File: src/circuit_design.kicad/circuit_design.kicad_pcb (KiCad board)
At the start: 2 copper layers, 220.3 x 182.9 mm, 184 parts, among them J1 CONN_BAT, Q1 BT136-600, Q2 BT136-600, Q3 BT136-600, Q4 BT136-600, U1 К176ИЕ12, U10 К155ЛА4, U11 К155ЛИ1, U12 К155ЛА1, U13 К155ИЕ5, U14 К155ЛЛ1, U15 К155ЛН1, U16 К155ЛИ1, U17 К155ТВ15, U18 К155ИЕ5, U19 К155ЛП5, U2 К155ЛП10, U20 К155ИВ1, U21 К155ИД7, U22 К155ИД4, U23 К155ЛН1, U24 К155ЛП10, U25 MOC3062M, U26 MOC3062M, U27 MOC3062M, U28 MOC3062M, U29 LM7806_TO220, U3 К155ЛЕ3, U30 SC6038, U31 К155ЛЕ1, U32 К155ЛН1, U33 К155ЛИ1, U34 К155ЛА4, U35 К155ТВ15, U36 К155ТЛ2, U37 4020, U38 LM7806_TO220, U39 К155ЛН1, U4 К155ЛН1, U5 К155ЛИ1, U6 К155ЛЛ1, U7 4020, U8 ICL7660, U9 К155ИЕ5, Y1 32768

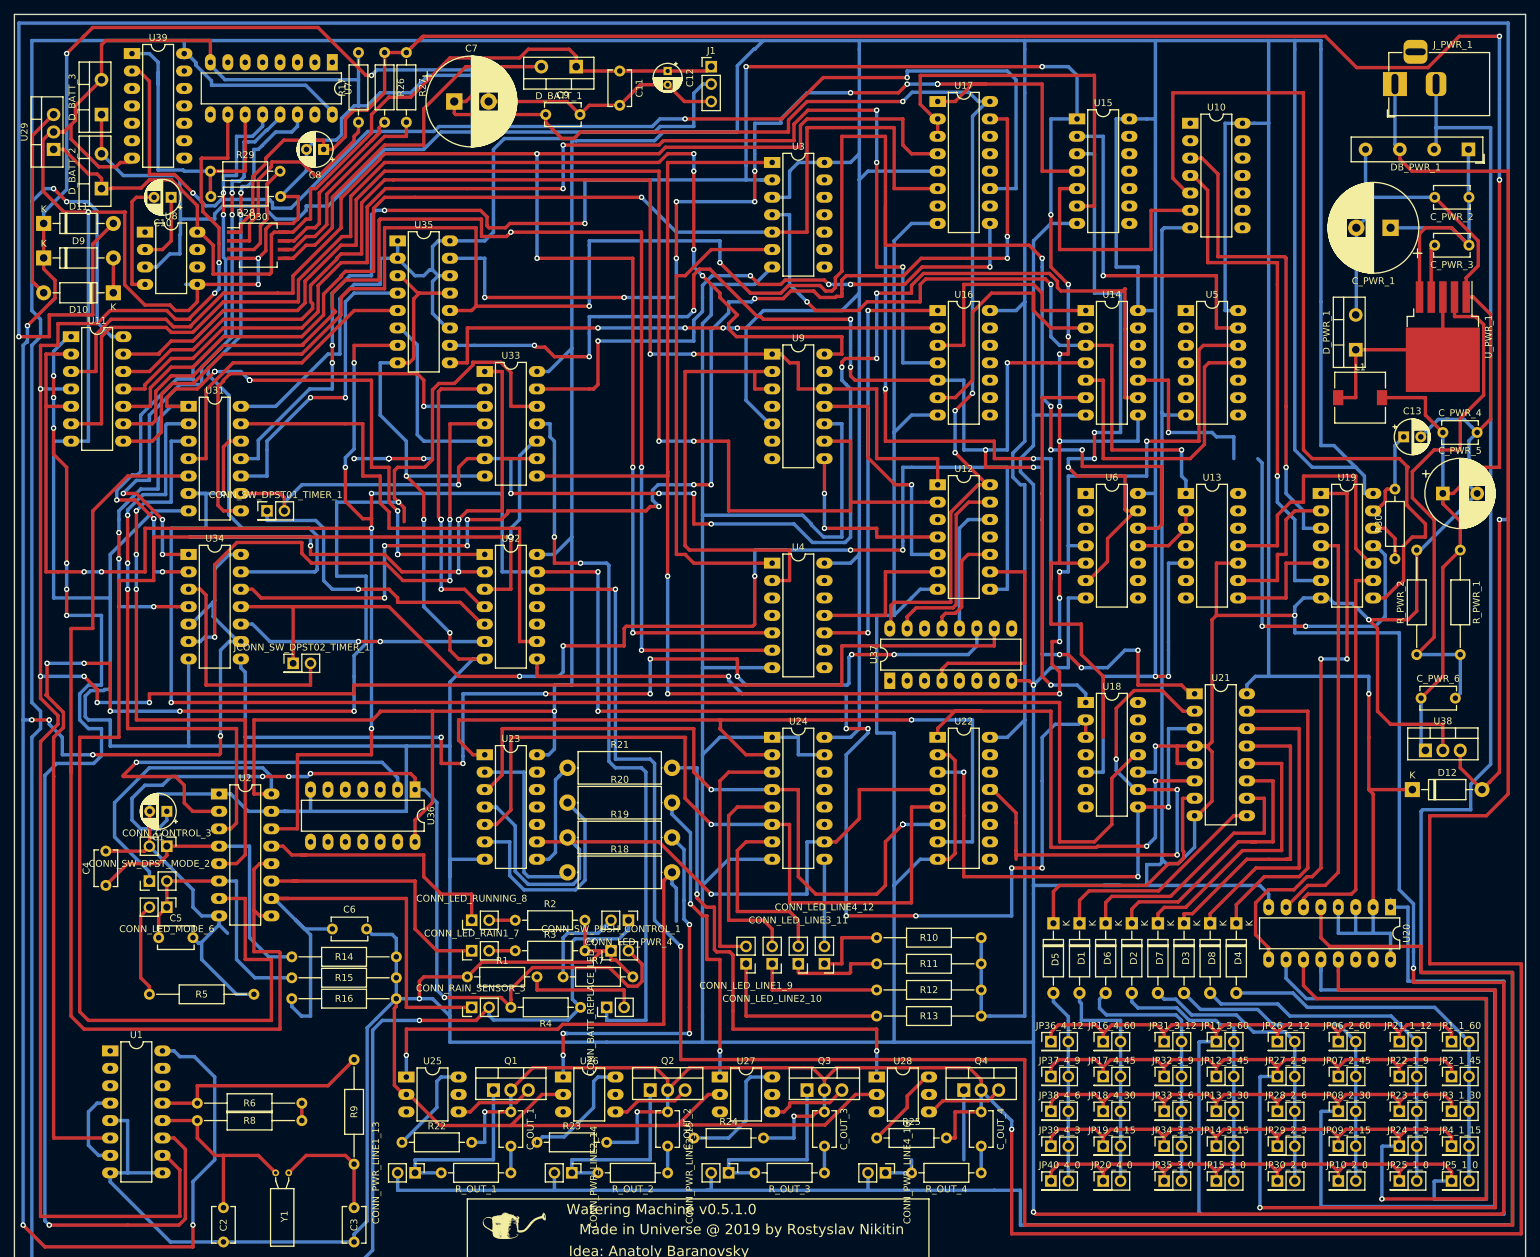
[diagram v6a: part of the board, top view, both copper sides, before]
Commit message: The PCB layout was fixed according to the rules.
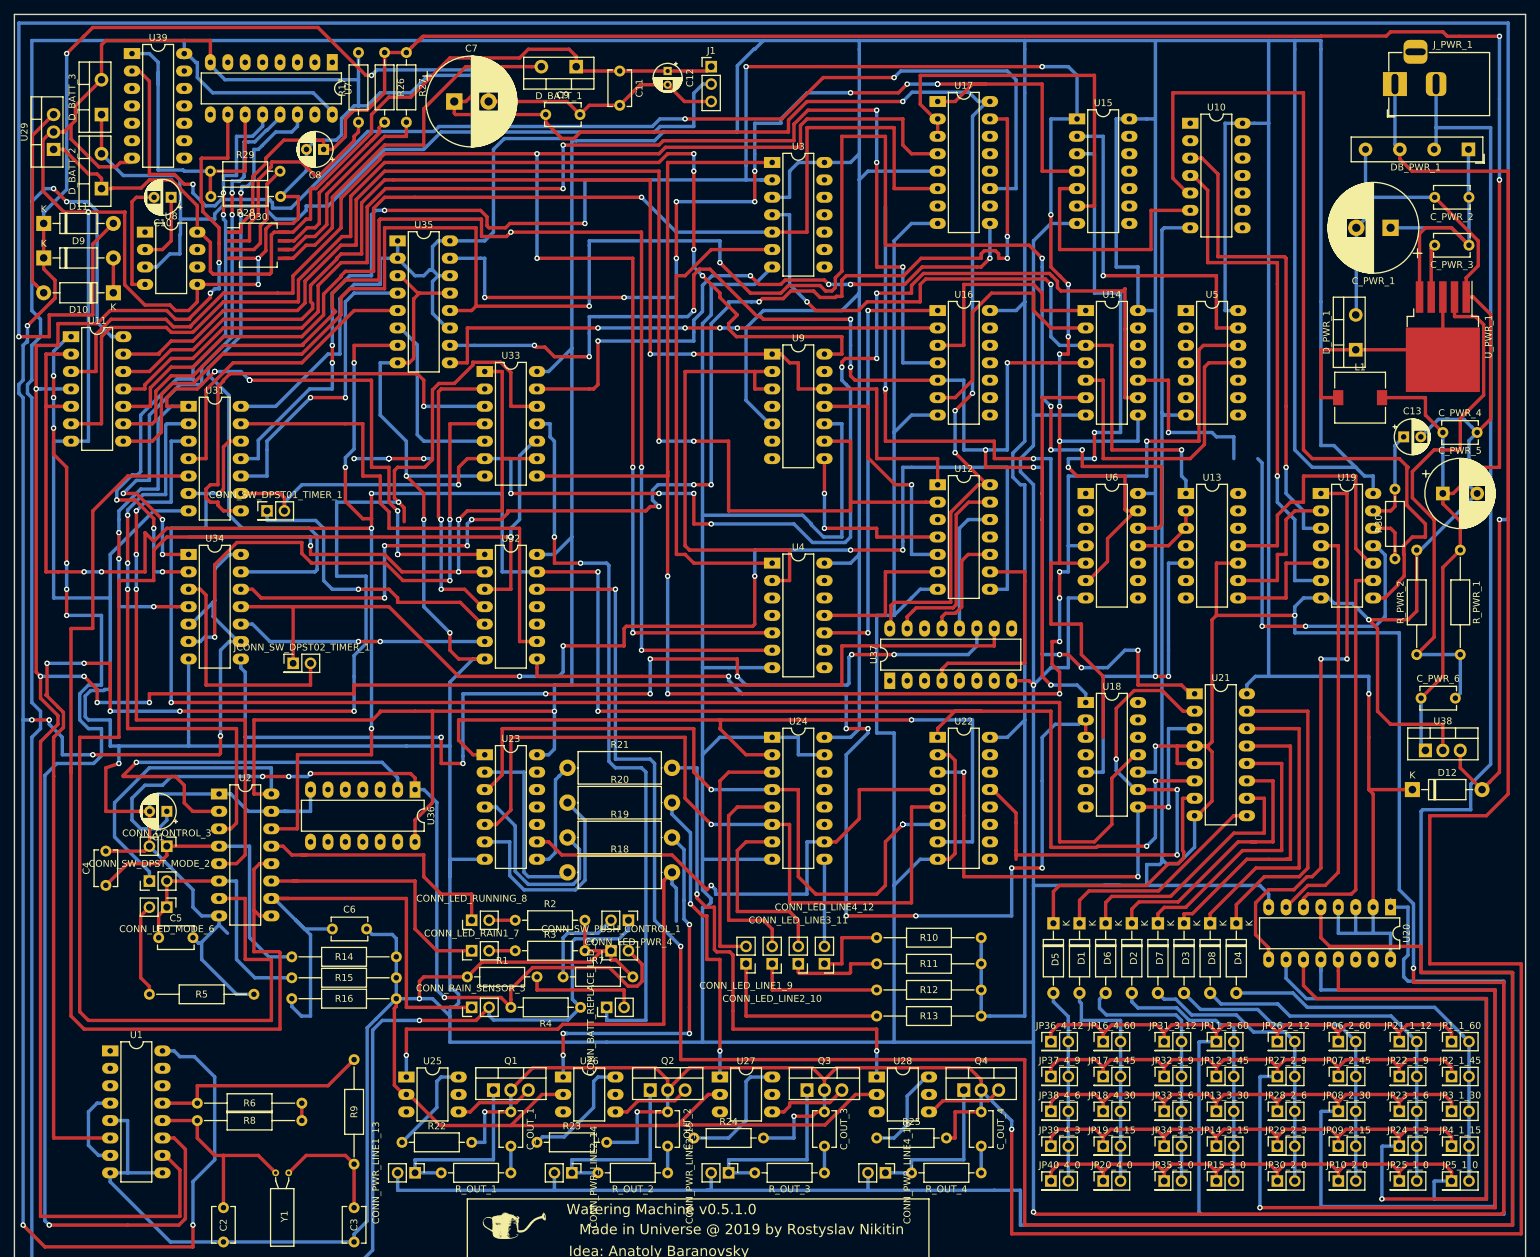
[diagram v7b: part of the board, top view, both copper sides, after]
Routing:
- net Net-(CONN_PWR_LINE4_16-Pad1): track 15.9 -> 23.5 mm
- net GND: track 2175.5 -> 2169.2 mm, vias 13 -> 14
- net Net-(D_PWR_1-Pad1): track 32.0 -> 37.1 mm
- net +9V: track 347.4 -> 344.1 mm
- net /Completed(In): track 223.3 -> 220.4 mm
- net Net-(U31-Pad8): track 64.9 -> 67.7 mm
- net +5V: track 1810.6 -> 1812.5 mm
- net CLK_MIN: track 379.4 -> 381.1 mm
- net Net-(R25-Pad1): track 12.3 -> 13.8 mm
- net Net-(U17-Pad15): track 182.0 -> 183.3 mm
- net Net-(U10-Pad5): track 128.9 -> 130.1 mm
- net /Mode(In): track 213.2 -> 212.0 mm
- net Net-(U22-Pad4): track 74.8 -> 75.7 mm
- net Net-(U17-Pad9): track 90.3 -> 89.6 mm
- net /Running(Out): track 380.0 -> 380.7 mm
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
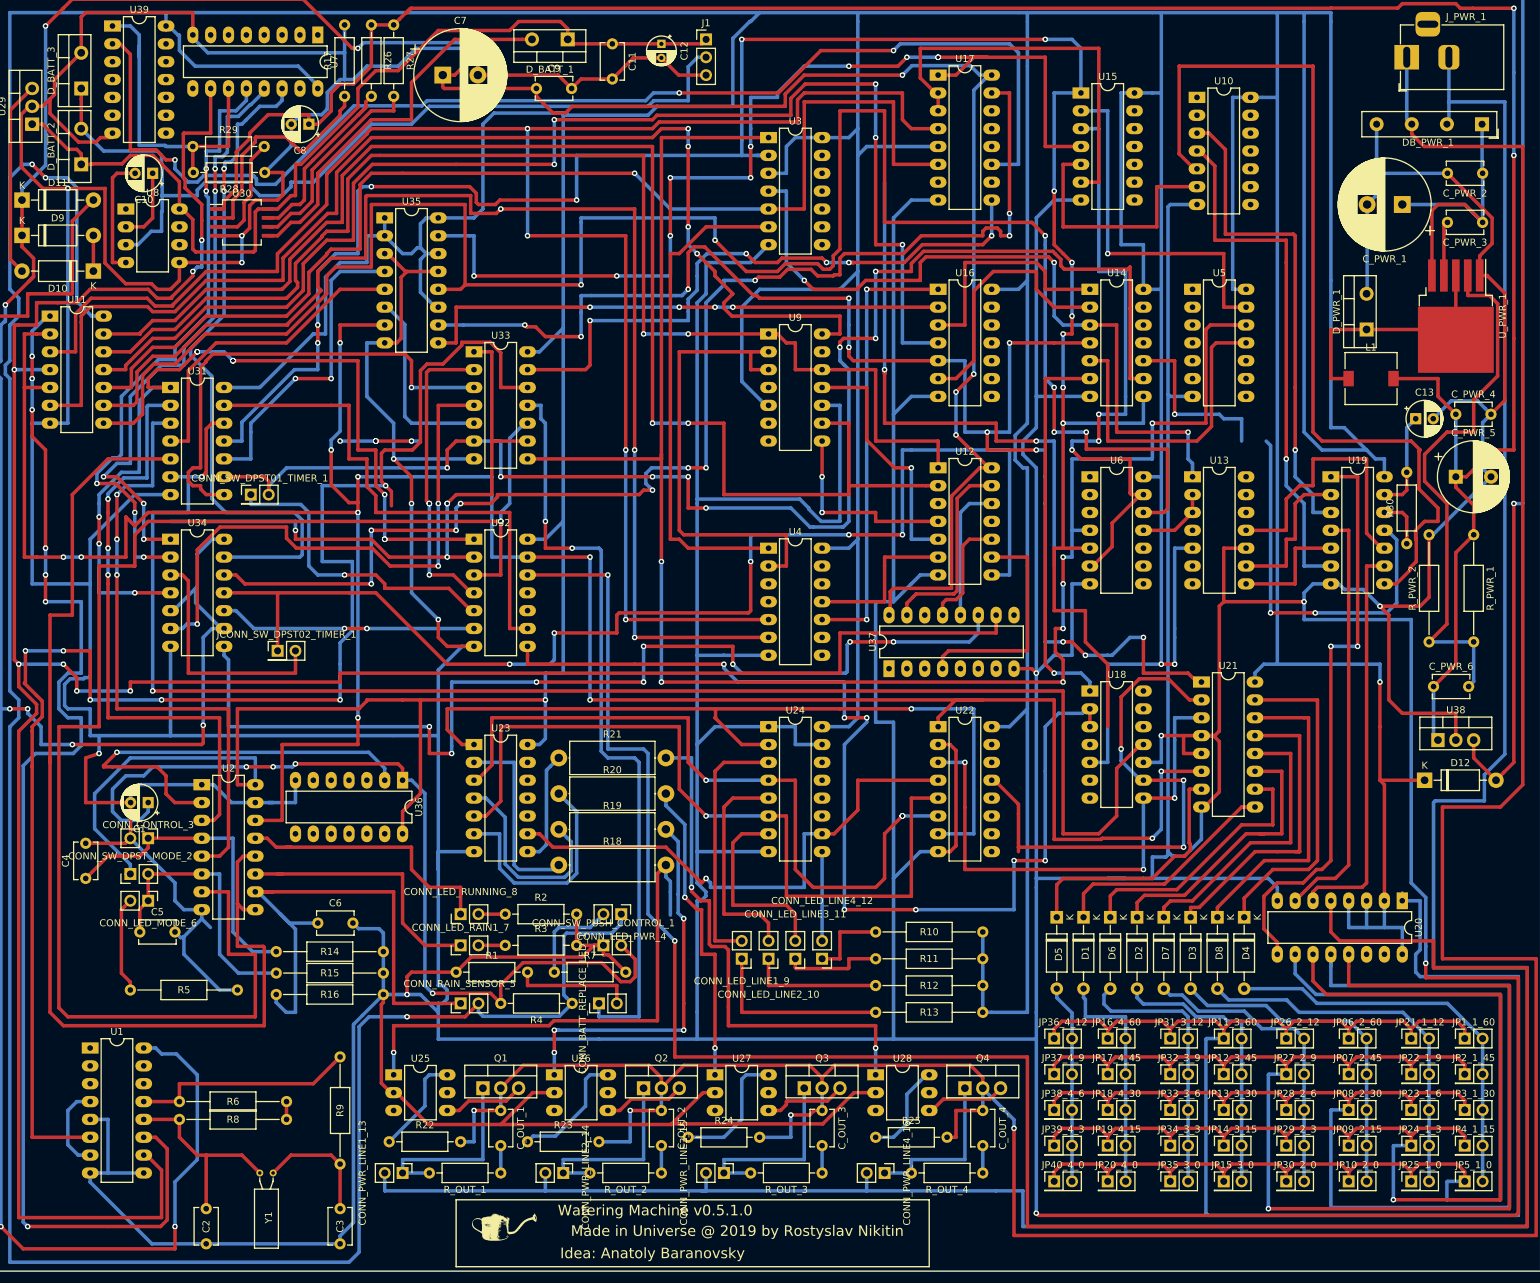
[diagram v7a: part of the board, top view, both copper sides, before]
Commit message: 01. The PCB layout was updated 02. The gerber files was updated 03. The README.md was initialized
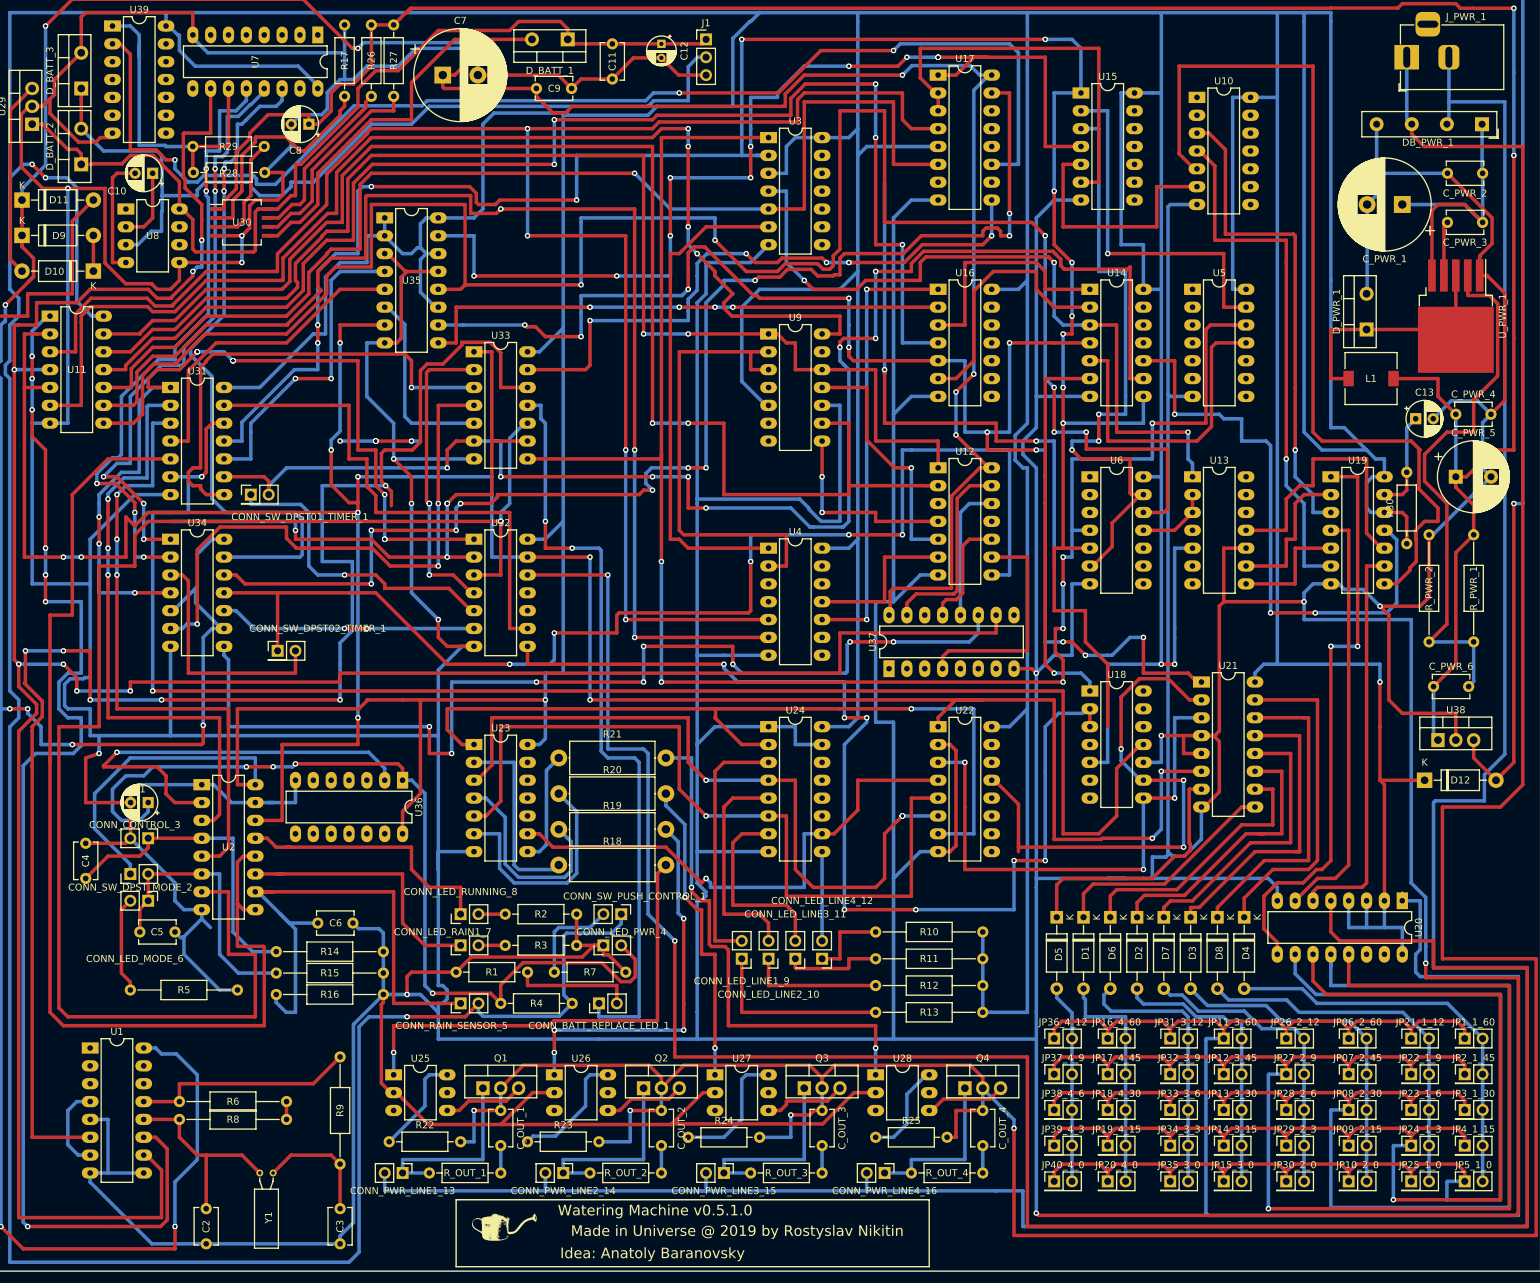
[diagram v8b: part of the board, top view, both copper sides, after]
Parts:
- renumbered JCONN_SW_DPST02_TIMER_1 to CONN_SW_DPST02_TIMER_1
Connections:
- R30 pad 1: Net-(R30-Pad1) -> +5V
- U1 pad 1: (no net) -> Net-(U1-Pad1)
- U1 pad 14: (no net) -> Net-(U1-Pad14)
- U1 pad 15: (no net) -> Net-(U1-Pad15)
- U1 pad 2: (no net) -> Net-(U1-Pad2)
- U1 pad 3: (no net) -> Net-(U1-Pad3)
- U13 pad 12: (no net) -> Net-(U13-Pad12)
- U13 pad 13: (no net) -> Net-(U13-Pad13)
- U13 pad 14: (no net) -> Net-(U13-Pad14)
- U13 pad 4: (no net) -> Net-(U13-Pad4)
- U13 pad 6: (no net) -> Net-(U13-Pad6)
- U13 pad 7: (no net) -> Net-(U13-Pad7)
- U17 pad 10: (no net) -> Net-(U17-Pad10)
- U17 pad 12: (no net) -> Net-(U17-Pad12)
- U17 pad 13: (no net) -> Net-(U17-Pad13)
- U17 pad 14: (no net) -> Net-(U17-Pad14)
- U17 pad 7: (no net) -> Net-(U17-Pad7)
- U18 pad 12: (no net) -> Net-(U18-Pad12)
- U18 pad 13: (no net) -> Net-(U18-Pad13)
- U18 pad 14: (no net) -> Net-(U18-Pad14)
- U18 pad 4: (no net) -> Net-(U18-Pad4)
- U18 pad 6: (no net) -> Net-(U18-Pad6)
- U18 pad 7: (no net) -> Net-(U18-Pad7)
- U19 pad 12: Net-(R30-Pad1) -> +5V
- U20 pad 14: (no net) -> Net-(U20-Pad14)
- U20 pad 15: (no net) -> Net-(U20-Pad15)
- U22 pad 10: (no net) -> Net-(U22-Pad10)
- U22 pad 11: (no net) -> Net-(U22-Pad11)
- U22 pad 12: (no net) -> Net-(U22-Pad12)
- U22 pad 14: (no net) -> Net-(U22-Pad14)
- U22 pad 15: (no net) -> Net-(U22-Pad15)
- U22 pad 9: (no net) -> Net-(U22-Pad9)
- U24 pad 11: (no net) -> Net-(U24-Pad11)
- U24 pad 12: (no net) -> Net-(U24-Pad12)
- U24 pad 13: (no net) -> Net-(U24-Pad13)
- U24 pad 14: (no net) -> Net-(U24-Pad14)
- U25 pad 3: (no net) -> Net-(U25-Pad3)
- U25 pad 5: (no net) -> Net-(U25-Pad5)
- U26 pad 3: (no net) -> Net-(U26-Pad3)
- U26 pad 5: (no net) -> Net-(U26-Pad5)
- U27 pad 3: (no net) -> Net-(U27-Pad3)
- U27 pad 5: (no net) -> Net-(U27-Pad5)
- U28 pad 3: (no net) -> Net-(U28-Pad3)
- U28 pad 5: (no net) -> Net-(U28-Pad5)
- U37 pad 1: (no net) -> Net-(U37-Pad1)
- U37 pad 14: (no net) -> Net-(U37-Pad14)
- U37 pad 2: (no net) -> Net-(U37-Pad2)
- U37 pad 3: (no net) -> Net-(U37-Pad3)
- U37 pad 5: (no net) -> Net-(U37-Pad5)
- U37 pad 6: (no net) -> Net-(U37-Pad6)
- U37 pad 7: (no net) -> Net-(U37-Pad7)
- U37 pad 9: (no net) -> Net-(U37-Pad9)
- U7 pad 1: (no net) -> Net-(U7-Pad1)
- U7 pad 15: (no net) -> Net-(U7-Pad15)
- U7 pad 2: (no net) -> Net-(U7-Pad2)
- U7 pad 3: (no net) -> Net-(U7-Pad3)
- U7 pad 4: (no net) -> Net-(U7-Pad4)
- U7 pad 5: (no net) -> Net-(U7-Pad5)
- U7 pad 6: (no net) -> Net-(U7-Pad6)
- U7 pad 7: (no net) -> Net-(U7-Pad7)
- U7 pad 9: (no net) -> Net-(U7-Pad9)
- U8 pad 1: (no net) -> Net-(U8-Pad1)
- U8 pad 6: (no net) -> Net-(U8-Pad6)
- U8 pad 7: (no net) -> Net-(U8-Pad7)
- U9 pad 13: (no net) -> Net-(U9-Pad13)
- U9 pad 4: (no net) -> Net-(U9-Pad4)
- U9 pad 6: (no net) -> Net-(U9-Pad6)
- U9 pad 7: (no net) -> Net-(U9-Pad7)
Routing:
- net +5V: track 1812.5 -> 1829.0 mm
- net Net-(R18-Pad2): track 74.8 -> 67.5 mm
- net Net-(R30-Pad1): track 7.25 -> 0.00 mm
- net Net-(U14-Pad10): track 79.5 -> 83.0 mm
